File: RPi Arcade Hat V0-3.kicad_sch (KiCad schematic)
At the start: 102 parts, among them J1 Raspberry_Pi_2_3, J10 Coin/Note Input, J11 +24V IN, J12 +12V OUT, J13 Player 1, J14 Player 2, J15 Player 3, J16 Player 4, J19 Coin Counter, J2 Player 1, J3 Player 2, J4 Spares, J5 Player 3, J6 Player 4, J7 +24V OUT, J8 Counter Bypass, Q1 BC847, Q10 BC847, Q11 BC847, Q12 BC847, Q13 BC847, Q14 BC847, Q15 BC847, Q16 BC847, Q2 BC847, Q3 BC847, Q4 BC847, Q5 BC847, Q6 BC847, Q7 BC847, Q8 BC847, Q9 BC847, U1 SN74HC32N, U10 NE555DR, U12 SN74HC08N, U13 NE555DR, U14 SN74HC74N, U18 SN74HC08N, U3 LM2595S-12

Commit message: Minor Refinements, and Final Gerbers
Made some final refinements, and made sure that silkscreens were also correct before getting PCB's made
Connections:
- net Column 2: no longer Q4.3 (C), Q5.3 (C), Q6.3 (C), Q7.3 (C)
- net Column 9: now reaches J1.27 (ID_SD/GPIO0)
- net Column 9: now also Q4.3 (C), Q5.3 (C), Q6.3 (C), Q7.3 (C)
- no-connect marks 20 -> 19
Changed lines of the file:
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@@
   (junction (at 359.41 204.47) (diameter 0) (color 0 0 0 0)
   )
-  (no_connect (at 68.58 29.21))
   (no_connect (at 68.58 31.75))
   (no_connect (at 27.94 67.31))
@@
     (stroke (width 0) (type default) (color 0 0 0 0))
   )
+  (wire (pts (xy 68.58 29.21) (xy 71.12 29.21))
+    (stroke (width 0) (type default) (color 0 0 0 0))
+  )
   (wire (pts (xy 125.73 34.29) (xy 125.73 40.64))
     (stroke (width 0) (type default) (color 0 0 0 0))
@@
     )
   )
+  (global_label "Column 9" (shape input) (at 71.12 29.21 0) (fields_autoplaced)
+    (effects (font (size 1.27 1.27)) (justify left))
+    (property "Intersheet References" "${INTERSHEET_REFS}" (id 0) (at 82.786 29.1306 0)
+      (effects (font (size 1.27 1.27)) (justify left) hide)
+    )
+  )
   (global_label "Row 2" (shape input) (at 25.4 57.15 180) (fields_autoplaced)
     (effects (font (size 1.27 1.27)) (justify right))
@@
     )
   )
-  (global_label "Column 2" (shape input) (at 246.38 73.66 0) (fields_autoplaced)
+  (global_label "Column 9" (shape input) (at 246.38 73.66 0) (fields_autoplaced)
     (effects (font (size 1.27 1.27)) (justify left))
     (property "Intersheet References" "${INTERSHEET_REFS}" (id 0) (at 258.046 73.5806 0)
@@
     )
   )
-  (global_label "Column 2" (shape input) (at 246.38 58.42 0) (fields_autoplaced)
+  (global_label "Column 9" (shape input) (at 246.38 58.42 0) (fields_autoplaced)
     (effects (font (size 1.27 1.27)) (justify left))
     (property "Intersheet References" "${INTERSHEET_REFS}" (id 0) (at 258.046 58.3406 0)
@@
     )
   )
-  (global_label "Column 2" (shape input) (at 246.38 43.18 0) (fields_autoplaced)
+  (global_label "Column 9" (shape input) (at 246.38 43.18 0) (fields_autoplaced)
     (effects (font (size 1.27 1.27)) (justify left))
     (property "Intersheet References" "${INTERSHEET_REFS}" (id 0) (at 258.046 43.1006 0)
@@
     )
   )
-  (global_label "Column 2" (shape input) (at 246.38 27.94 0) (fields_autoplaced)
+  (global_label "Column 9" (shape input) (at 246.38 27.94 0) (fields_autoplaced)
     (effects (font (size 1.27 1.27)) (justify left))
     (property "Intersheet References" "${INTERSHEET_REFS}" (id 0) (at 258.046 27.8606 0)

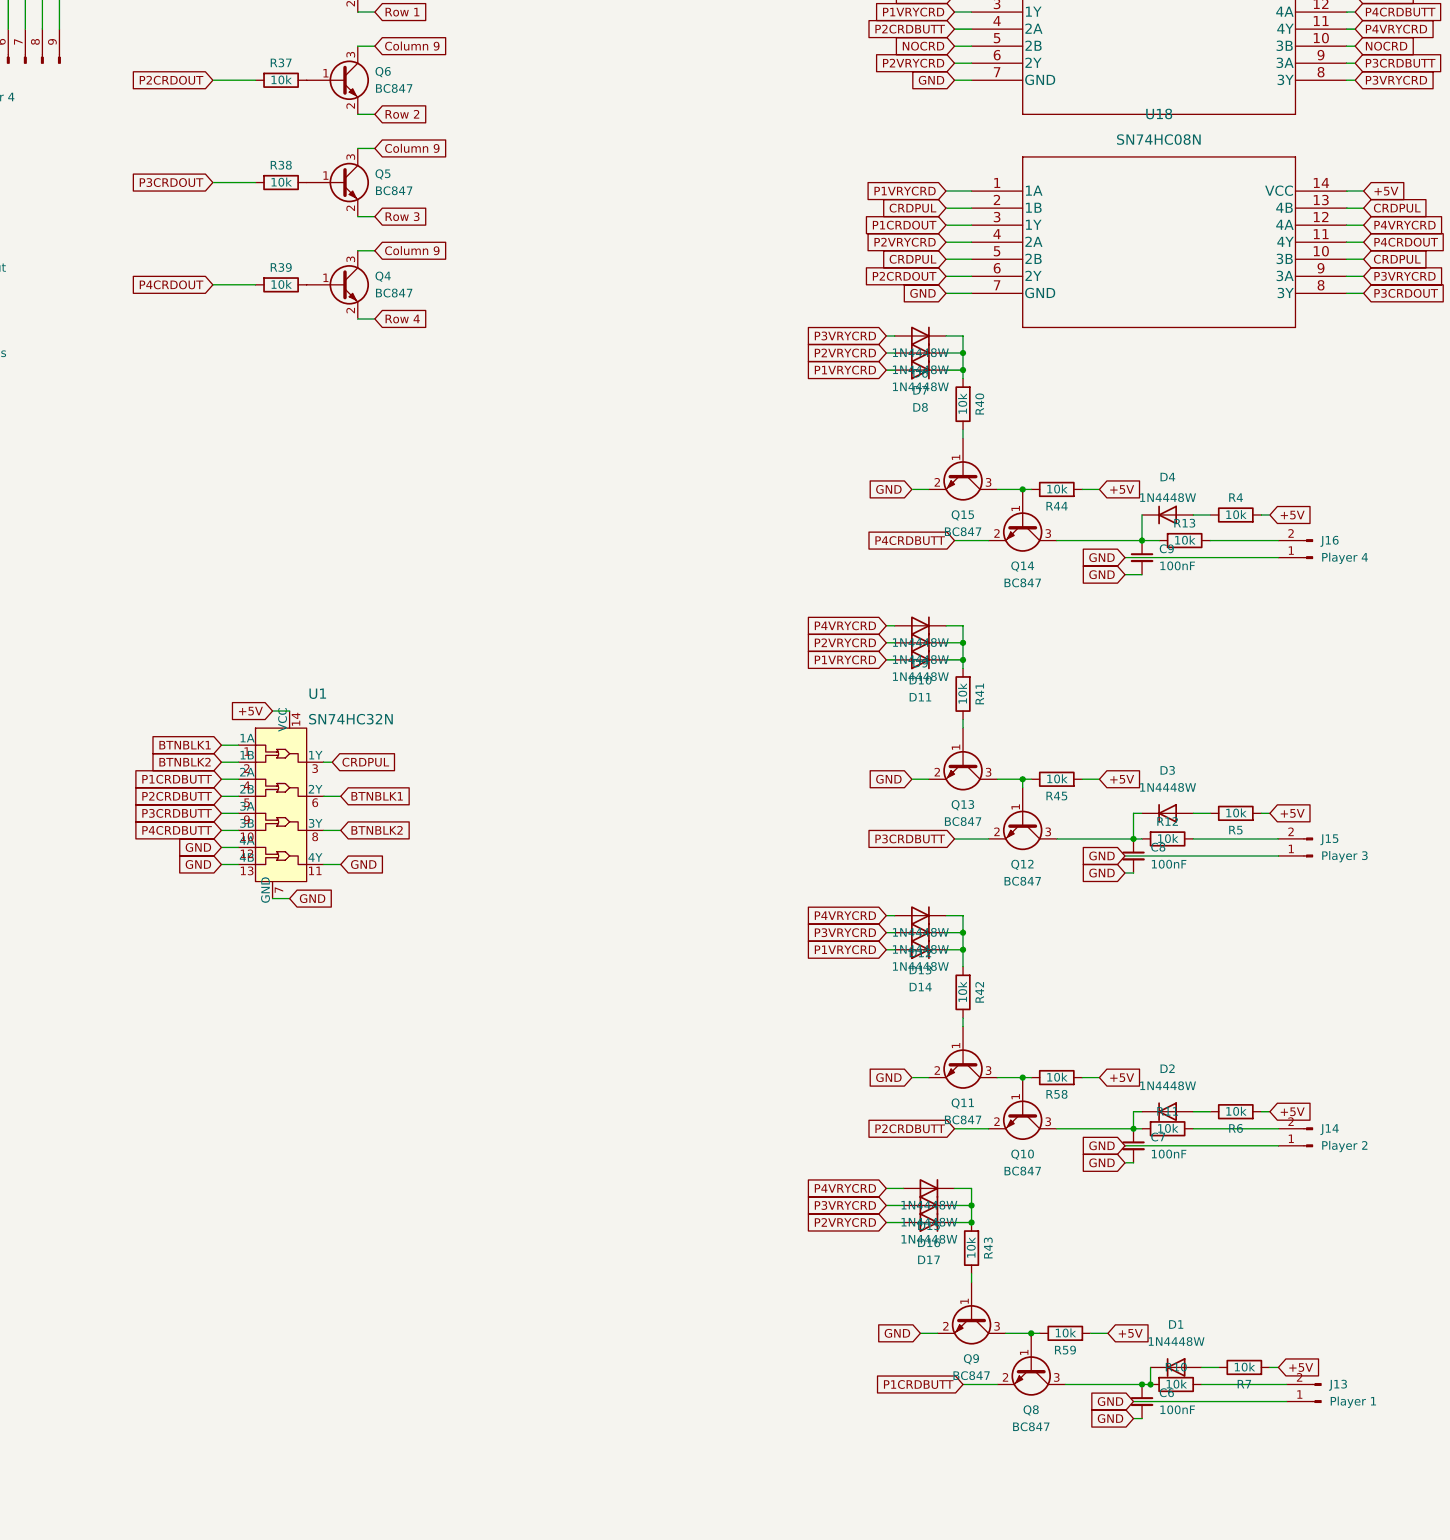
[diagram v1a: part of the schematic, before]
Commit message: Found Error on Debounce Circuit
As I was going through the schematic I found I wired the button credit input incorrect, and had the logic level held high then pulling to GND, and I should've used an inverter on the output, went with a simple fix, and ended up removing the extra components and changing the connection on the button from GND to +5V
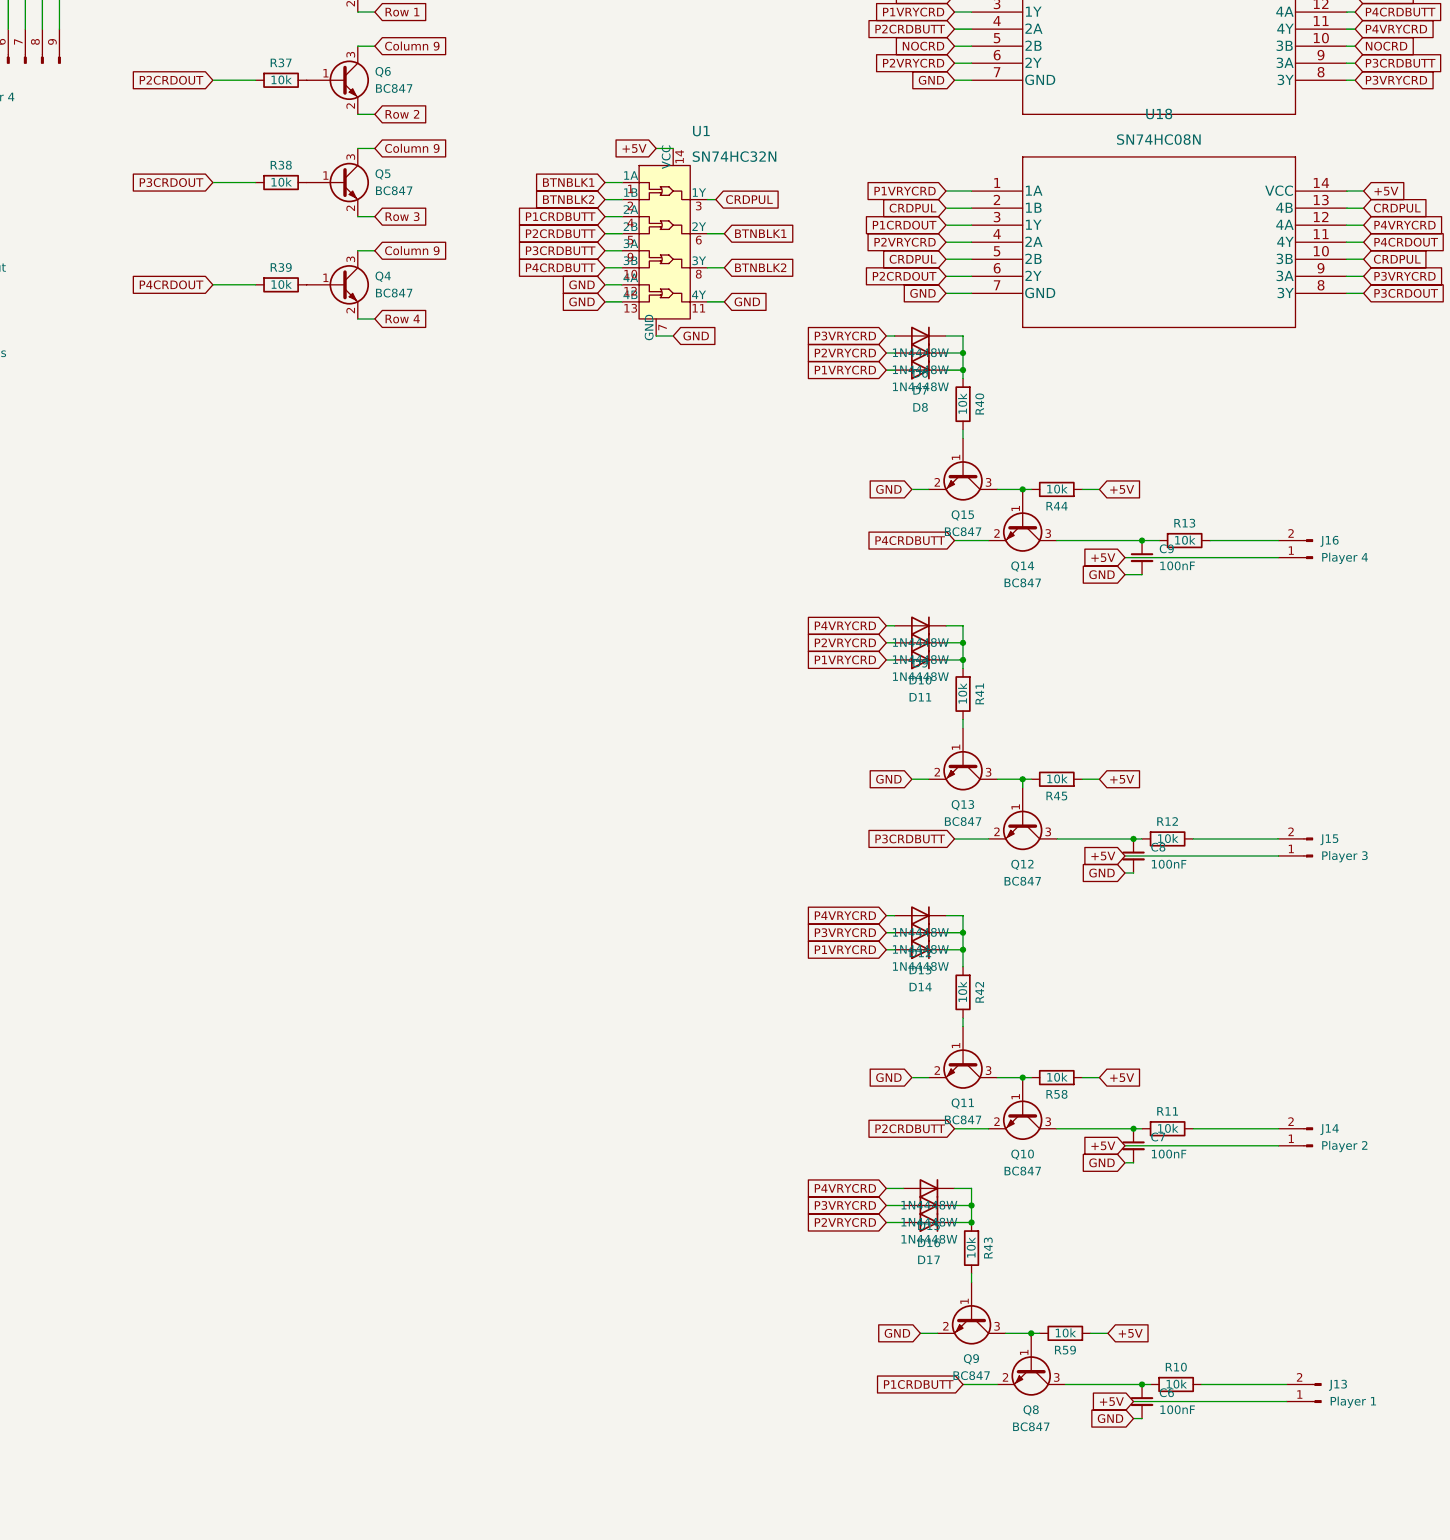
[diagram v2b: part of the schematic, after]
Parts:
- removed D1, D2, D3, D4: 1N4448W, Diode_SMD:D_SOD-123, symbol Diode:1N4448W
- removed R4, R5, R6, R7: 10k, Resistor_SMD:R_1206_3216Metric, symbol Device:R
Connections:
- net +5V: now also J13.1 (Pin_1), J14.1 (Pin_1), J15.1 (Pin_1), J16.1 (Pin_1)
- net GND: no longer J13.1 (Pin_1), J14.1 (Pin_1), J15.1 (Pin_1), J16.1 (Pin_1)
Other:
- moved on the sheet: U1

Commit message: Reverted Changes
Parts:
- added D1, D2, D3, D4: 1N4448W, Diode_SMD:D_SOD-123, symbol Diode:1N4448W
- added R4, R5, R6, R7: 10k, Resistor_SMD:R_1206_3216Metric, symbol Device:R
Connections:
- net +5V: now also R4.2, R5.2, R6.2, R7.2; no longer J13.1 (Pin_1), J14.1 (Pin_1), J15.1 (Pin_1), J16.1 (Pin_1)
- net GND: now also J13.1 (Pin_1), J14.1 (Pin_1), J15.1 (Pin_1), J16.1 (Pin_1)
- net at C6.1, Q8.3 (C), R10.2: now also D1.1 (K)
- net at C7.1, Q10.3 (C), R11.2: now also D2.1 (K)
- net at C8.1, Q12.3 (C), R12.2: now also D3.1 (K)
- net at C9.1, Q14.3 (C), R13.2: now also D4.1 (K)
- new net: D2.2 (A), R6.1
- new net: D1.2 (A), R7.1
- new net: D3.2 (A), R5.1
- new net: D4.2 (A), R4.1
